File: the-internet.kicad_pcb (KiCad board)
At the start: 2 copper layers, 88 x 40 mm, 8 parts, among them J1 POWER, J2 LOLIN-C3-MINI (L), J3 LOLIN-C3-MINI (R), Q1 DMP2004K, Q2 DMP2004K

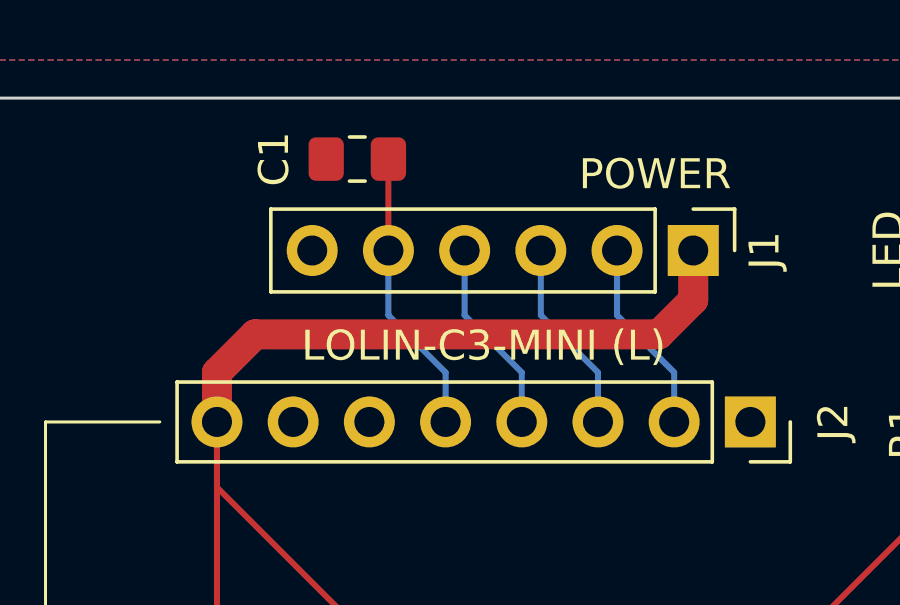
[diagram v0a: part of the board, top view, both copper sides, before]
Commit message: Remove ADC divider control
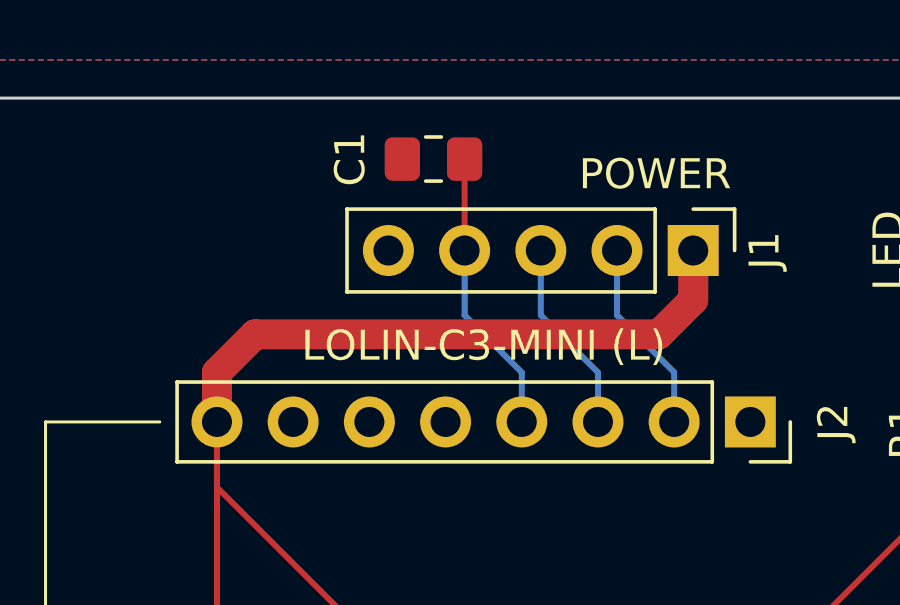
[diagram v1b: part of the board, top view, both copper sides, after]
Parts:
- J1: footprint Connector_PinHeader_2.54mm:PinHeader_1x06_P2.54mm_Vertical -> Connector_PinHeader_2.54mm:PinHeader_1x05_P2.54mm_Vertical
- moved C1 2.54 mm to (46.0, 27.4)
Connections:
- C1 pad 1: CAPACITOR_VOLTAGE/GPIO0 -> CAPACITOR_VOLTAGE/GPIO1
- J1 pad 4: ~{MEASURE_VOLTAGE}/GPIO1 -> CAPACITOR_VOLTAGE/GPIO1
- J1 pad 5: CAPACITOR_VOLTAGE/GPIO0 -> GND
- J2 pad 4: ~{MEASURE_VOLTAGE}/GPIO1 -> CAPACITOR_VOLTAGE/GPIO1
- J2 pad 5: CAPACITOR_VOLTAGE/GPIO0 -> unconnected-(J2-Pin_5-Pad5)
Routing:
- net CAPACITOR_VOLTAGE/GPIO1: track 0.00 -> 9.55 mm
- net CAPACITOR_VOLTAGE/GPIO0: track 9.55 -> 0.00 mm
- net ~{MEASURE_VOLTAGE}/GPIO1: track 6.50 -> 0.00 mm

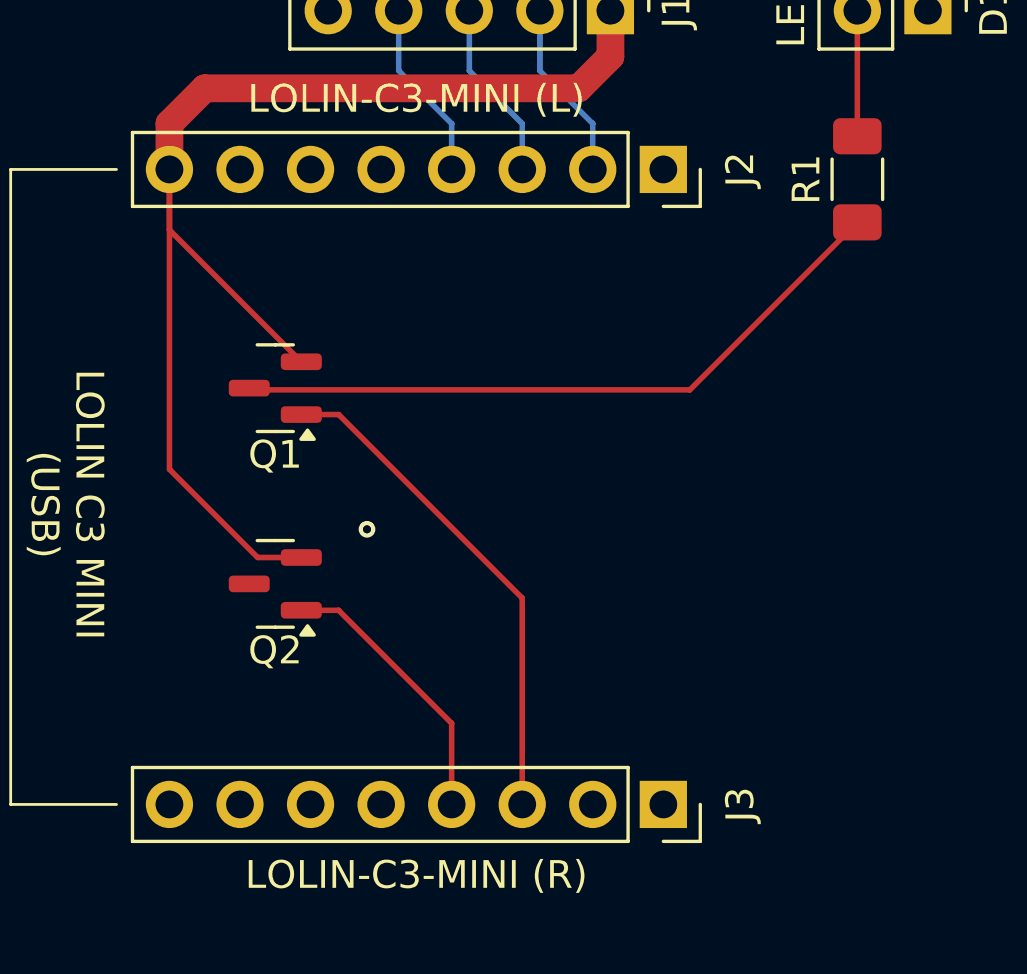
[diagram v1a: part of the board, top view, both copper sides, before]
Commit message: Use the better SOT-23-3 footprint for Q1, Q2
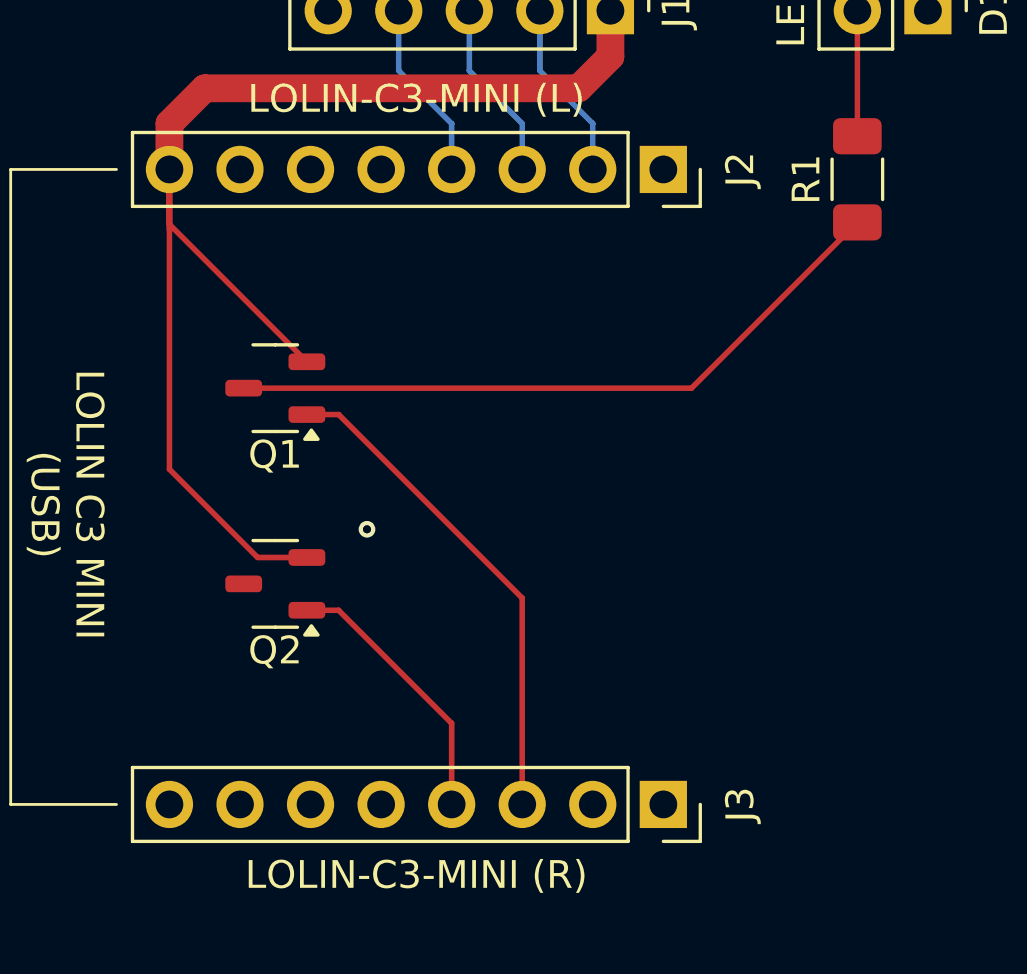
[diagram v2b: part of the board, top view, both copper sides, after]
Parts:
- Q1, Q2: footprint Package_TO_SOT_SMD:SOT-23 -> Package_TO_SOT_SMD:SOT-23-3
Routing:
- net +3.3V: track 45.9 -> 48.4 mm

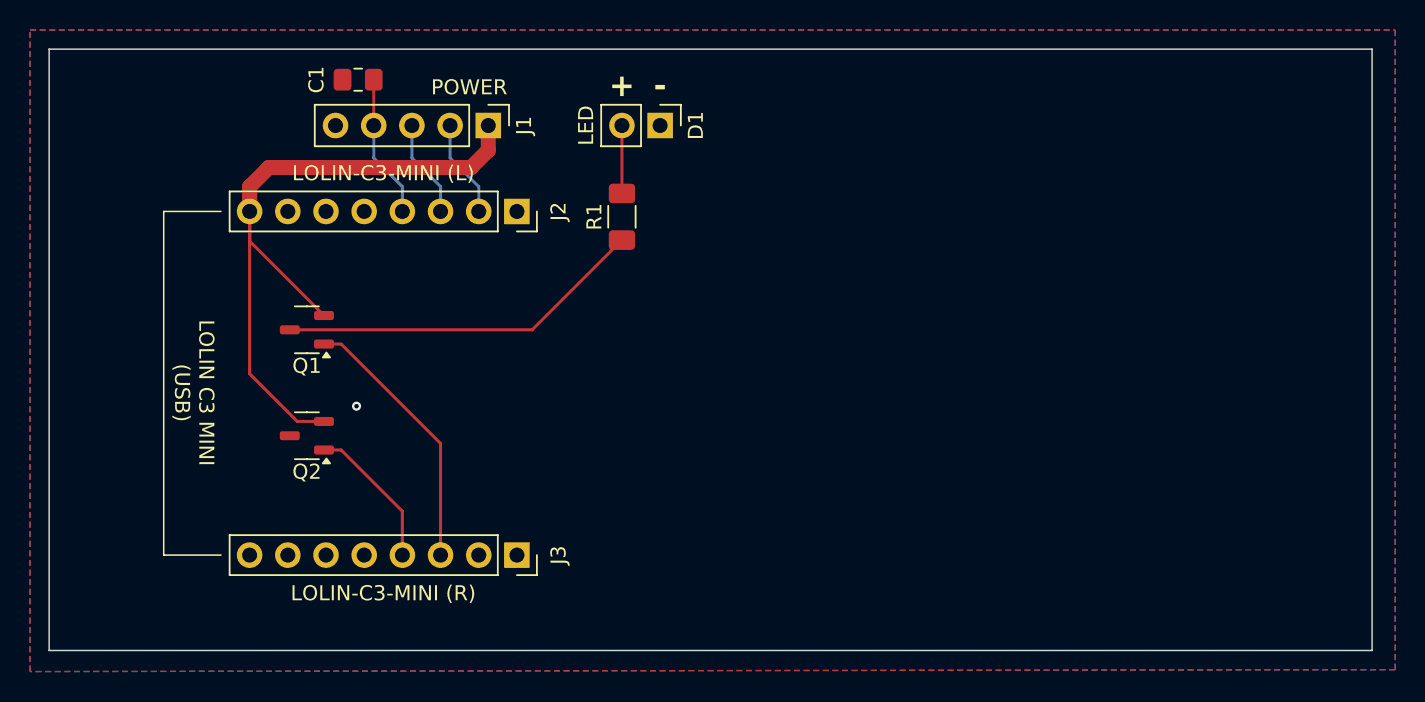
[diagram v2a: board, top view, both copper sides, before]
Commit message: Place buzzer, remove MOSFETs
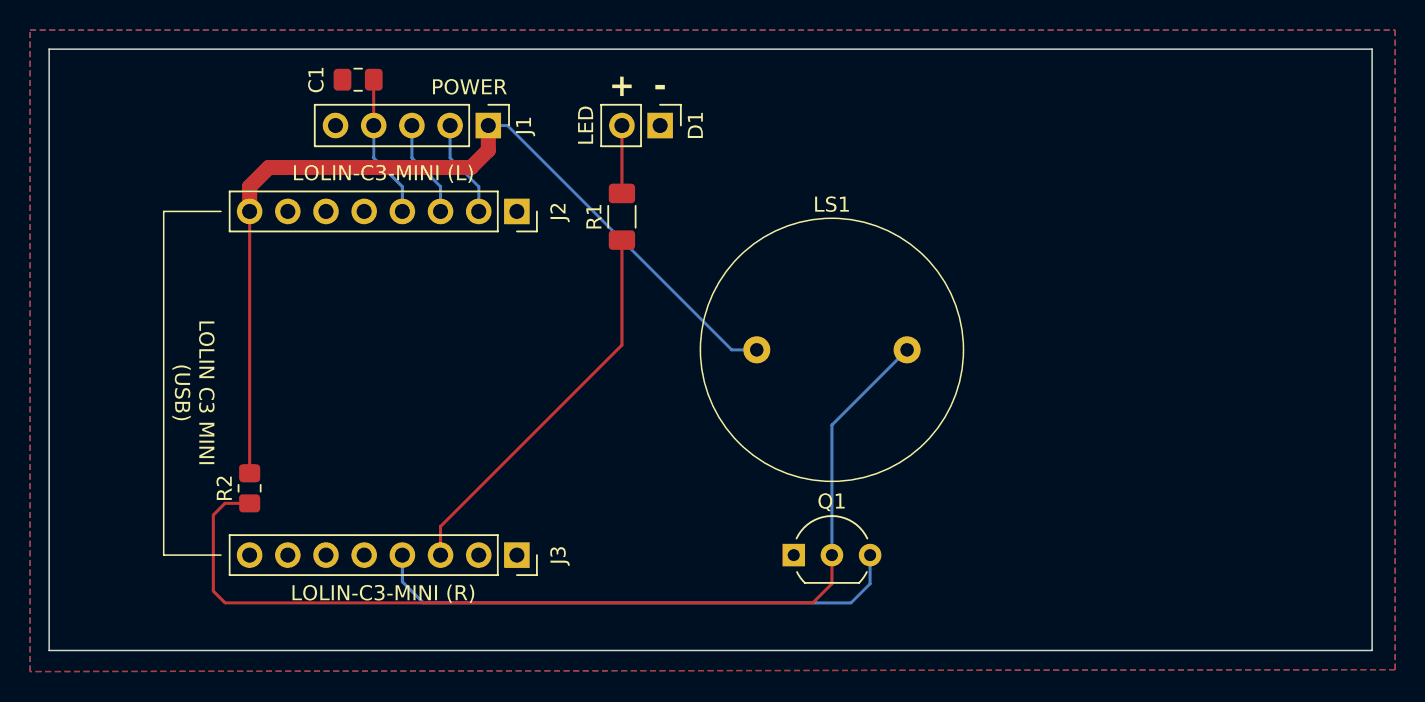
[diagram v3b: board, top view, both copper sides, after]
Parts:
- removed Q2: DMP2004K, Package_TO_SOT_SMD:SOT-23-3
- added LS1: PS1720P02, the-internet:PS1720P02, F.Cu at (77.5, 45.4)
- added R2: 1kΩ 1% 125mW, Resistor_SMD:R_0805_2012Metric_Pad1.20x1.40mm_HandSolder, F.Cu at (38.7, 54.6)
- Q1: value DMP2004K -> KSC1815YTA; footprint Package_TO_SOT_SMD:SOT-23-3 -> Package_TO_SOT_THT:TO-92_Inline_Wide
- R1: value 47Ω 1% 0.5W -> 47Ω 1% 250mW
- moved Q1 35.7 mm to (74.9, 59.1), turned to 0 degrees
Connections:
- Q1 pad 1: TOP_LED/GPIO10 -> GND
- Q1 pad 2: +3.3V -> Net-(Q1-C)
- Q1 pad 3: Net-(Q1-D) -> BUZZER/GPIO8
- R1 pad 1: Net-(Q1-D) -> TOP_LED/GPIO10
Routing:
- net Net-(Q1-C): track 0.00 -> 67.4 mm
- net BUZZER/GPIO8: track 9.82 -> 35.9 mm
- net Net-(Q1-D): track 24.6 -> 0.00 mm
- net +3.3V: track 48.4 -> 61.6 mm
- net TOP_LED/GPIO10: track 17.9 -> 26.0 mm
- net GND: vias 1 -> 0

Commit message: Add memes
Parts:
- added CAKE: LOGO, LOGO, F.Cu at (33.7, 30.5)
- added TROLLFACE: LOGO, LOGO, F.Cu at (102.9, 57.1)
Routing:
- net +3.3V: track 61.6 -> 64.6 mm
- net Net-(Q1-C): track 67.4 -> 68.3 mm
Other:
- board text added: "1993 1994 1996 1997 1998 1999 2000 2001 2002 2003 2004 2005 2006 2007 2008 2009 2010 2011 2012 2013 2014 2015"
- board text added: "2016 2017 2018 2019 2020 2021 2022 2023 2024"
- board text added: "September X, 1993 Das gibt's doch gar nicht {dblquote}Toddler with Diaper{dblquote} Model #5653 It's over 9000! Hampster Dance All your base are belong to us UwU You're The Man Now, Dog! Every time you masturbate... God kills a kitten Badger Badger Badger You Wouldn't Steal a Car Chuck Norris can divide by zero Downfall Never Gonna Give You Up Loss | || || |_ All Star (Shrek) PogChamp Nyan Cat Is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"
- board text added: "This is fine Distracted boyfriend Galaxy Brain Sir, this is a Wendy's Soyjaks vs. Chads amogus (sus) Girl Explaining You Like Kissing Boys Don't You A Circle?? In the Triangle Factory??"
- board text added: "https://github.com/nomis/the-internet-pcb"
- board text added: "urn:oid:1.3.6.1.4.1.39777.1.3.3.2.0"

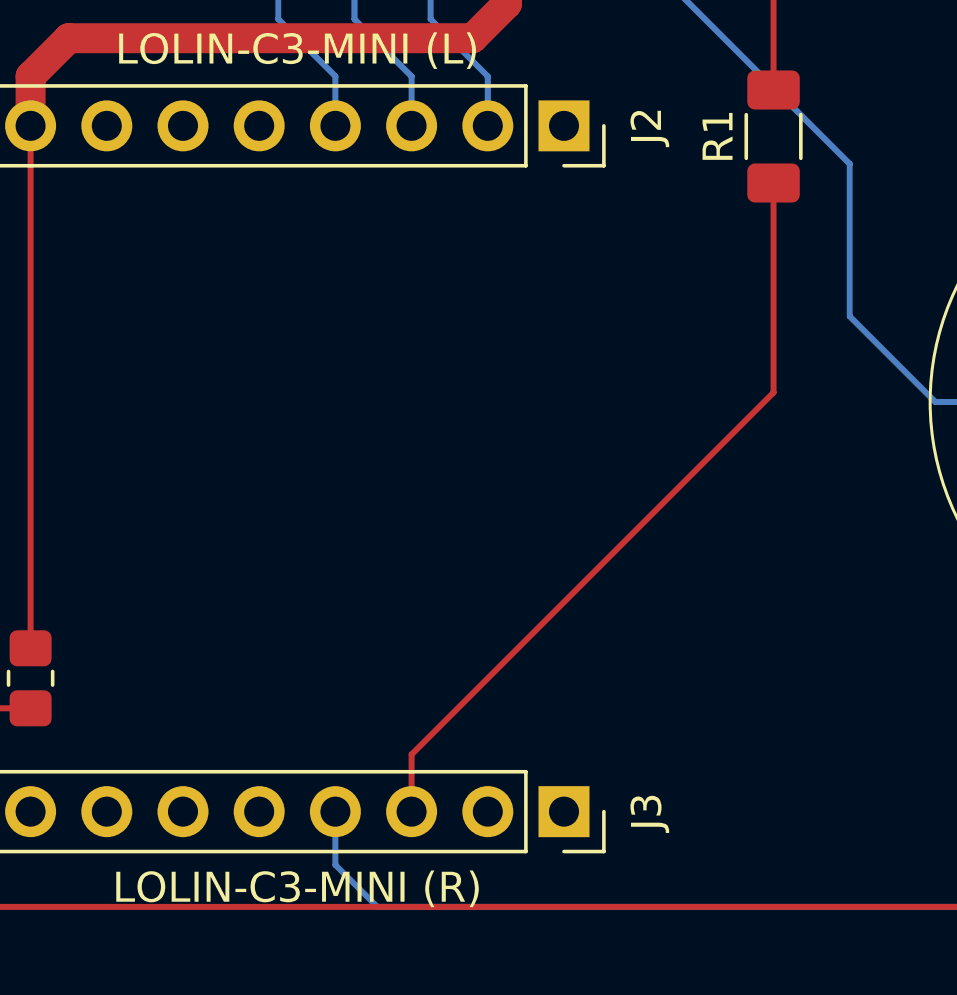
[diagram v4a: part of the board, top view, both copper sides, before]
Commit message: Move top LED to GPIO6 because GPIO10 has a glitch on powerup
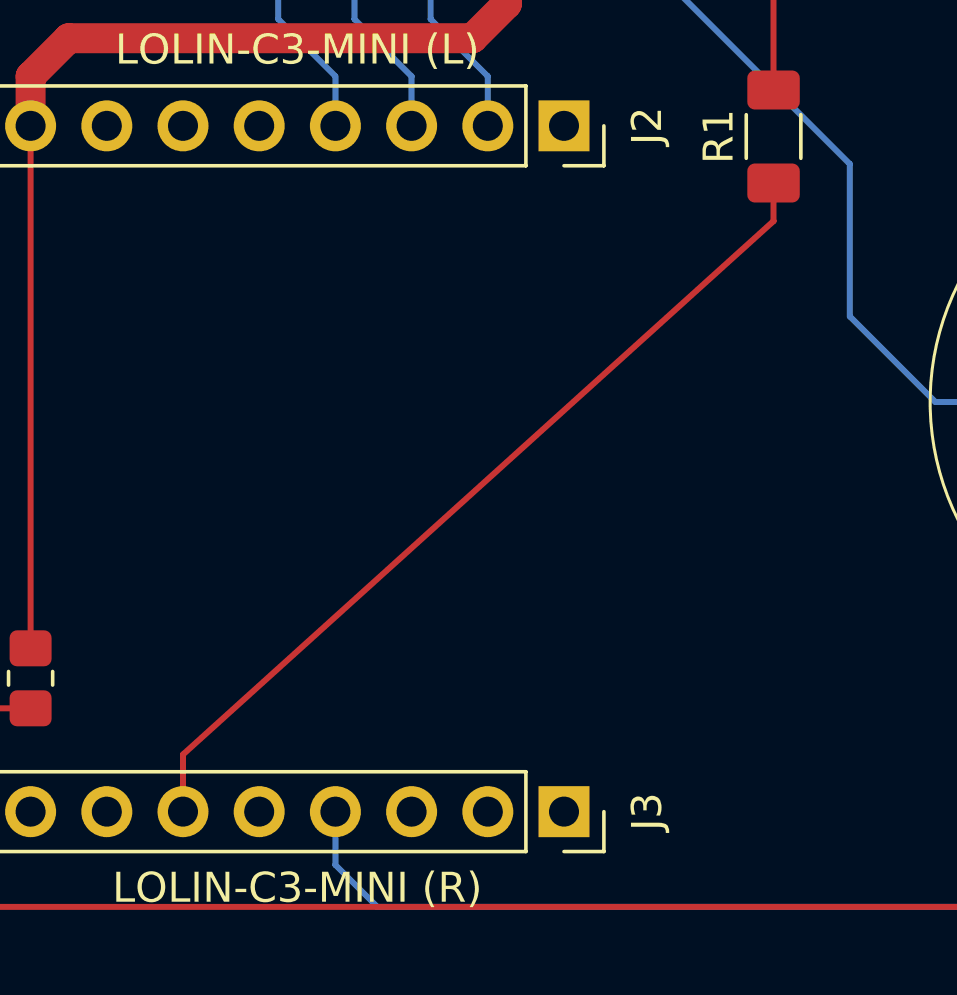
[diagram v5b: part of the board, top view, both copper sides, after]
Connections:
- J3 pad 3: TOP_LED/GPIO10 -> unconnected-(J3-Pin_3-Pad3)
- J3 pad 6: unconnected-(J3-Pin_6-Pad6) -> TOP_LED/GPIO6
- R1 pad 1: TOP_LED/GPIO10 -> TOP_LED/GPIO6
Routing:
- net TOP_LED/GPIO6: track 0.00 -> 29.7 mm
- net TOP_LED/GPIO10: track 26.0 -> 0.00 mm
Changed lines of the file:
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@@
 	(net 4 "unconnected-(J3-Pin_5-Pad5)")
 	(net 5 "unconnected-(J3-Pin_8-Pad8)")
-	(net 6 "TOP_LED{slash}GPIO10")
+	(net 6 "unconnected-(J3-Pin_3-Pad3)")
 	(net 7 "unconnected-(J3-Pin_1-Pad1)")
 	(net 8 "BUZZER{slash}GPIO8")
-	(net 9 "unconnected-(J3-Pin_6-Pad6)")
+	(net 9 "TOP_LED{slash}GPIO6")
 	(net 10 "unconnected-(J3-Pin_2-Pad2)")
 	(net 11 "~{EXTERNAL_POWER_PRESENT}{slash}GPIO3")
@@
 			)
 		)
-		(property "Datasheet" ""
+		(property "Datasheet" "https://product.tdk.com/en/system/files/dam/doc/product/sw_piezo/sw_piezo/piezo-buzzer/catalog/piezoelectronic_buzzer_ps_en.pdf"
 			(at 0 0 0)
 			(unlocked yes)
@@
 			)
 		)
-		(property "Description" ""
+		(property "Description" "Crystal speaker/transducer"
 			(at 0 0 0)
 			(unlocked yes)
@@
 			(layers "*.Cu" "*.Mask")
 			(remove_unused_layers no)
-			(net 6 "TOP_LED{slash}GPIO10")
+			(net 6 "unconnected-(J3-Pin_3-Pad3)")
 			(pinfunction "Pin_3")
-			(pintype "passive")
+			(pintype "passive+no_connect")
 		)
 		(pad "4" thru_hole circle
@@
 			(layers "*.Cu" "*.Mask")
 			(remove_unused_layers no)
-			(net 9 "unconnected-(J3-Pin_6-Pad6)")
+			(net 9 "TOP_LED{slash}GPIO6")
 			(pinfunction "Pin_6")
-			(pintype "passive+no_connect")
+			(pintype "passive")
 		)
 		(pad "7" thru_hole circle
@@
 			(layers "F.Cu" "F.Mask" "F.Paste")
 			(roundrect_rratio 0.192308)
-			(net 6 "TOP_LED{slash}GPIO10")
+			(net 9 "TOP_LED{slash}GPIO6")
 			(pintype "passive")
 		)
@@
 	)
 	(segment
-		(start 63.5 38.1)
-		(end 63.5 45.085)
-		(width 0.2)
-		(layer "F.Cu")
-		(net 6)
-	)
-	(segment
-		(start 51.435 57.15)
-		(end 51.435 59.055)
-		(width 0.2)
-		(layer "F.Cu")
-		(net 6)
-	)
-	(segment
-		(start 63.5 45.085)
-		(end 51.435 57.15)
-		(width 0.2)
-		(layer "F.Cu")
-		(net 6)
-	)
-	(segment
 		(start 78.74 62.23)
 		(end 50.292001 62.23)
@@
 	)
 	(segment
+		(start 63.5 38.1)
+		(end 63.5 39.37)
+		(width 0.2)
+		(layer "F.Cu")
+		(net 9)
+	)
+	(segment
+		(start 43.815 57.15)
+		(end 43.815 59.055)
+		(width 0.2)
+		(layer "F.Cu")
+		(net 9)
+	)
+	(segment
+		(start 63.5 39.37)
+		(end 43.815 57.15)
+		(width 0.2)
+		(layer "F.Cu")
+		(net 9)
+	)
+	(segment
